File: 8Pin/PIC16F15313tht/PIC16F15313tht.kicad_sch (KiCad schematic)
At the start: 17 parts, among them J1 JACK DC, J2 USB_B, J3 TERMINAL BLOCK, J4 POWER HEADERS, J5 Conn_02x04_Odd_Even, J6 Conn_02x04_Odd_Even, J7 ICSP, SW1 RESET, SW2 CONTROL, U1 PIC16F15313

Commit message: avance de actualización del proyecto
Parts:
- removed J4: POWER HEADERS, Connector_PinSocket_2.54mm:PinSocket_2x02_P2.54mm_Vertical, symbol Connector_Generic:Conn_02x02_Counter_Clockwise
- removed J5: Conn_02x04_Odd_Even, Connector_PinSocket_2.54mm:PinSocket_2x04_P2.54mm_Vertical, symbol Connector_Generic:Conn_02x04_Odd_Even
- removed J7: ICSP, Connector_PinHeader_2.54mm:PinHeader_1x06_P2.54mm_Horizontal, symbol Connector_Generic:Conn_01x06
- removed U1: PIC16F15313, Package_DIP:DIP-8_W7.62mm_Socket_LongPads, symbol MGV:PIC16F15313
- added C1: C, Capacitor_THT:C_Disc_D5.0mm_W2.5mm_P5.00mm, symbol Device:C
- added J4: Conn_02x02_Odd_Even, Connector_PinHeader_2.54mm:PinHeader_2x02_P2.54mm_Vertical, symbol Connector_Generic:Conn_02x02_Odd_Even
- added J5: ICSP, Connector_PinHeader_2.54mm:PinHeader_1x06_P2.54mm_Horizontal, symbol Connector_Generic:Conn_01x06
- added J7: terminales, Connector_PinHeader_2.54mm:PinHeader_2x04_P2.54mm_Vertical, symbol Connector_Generic:Conn_02x04_Odd_Even
- added U1: PIC16F15313, Package_DIP:DIP-8_W7.62mm, symbol CreatedSimbols:PIC16F15313
- D2: value LED_ON -> LED
- D3: value LED_OP -> LED OP
- J1: footprint Connector_BarrelJack:BarrelJack_Kycon_KLDX-0202-xC_Horizontal -> Connector_BarrelJack:BarrelJack_Horizontal
- J2: footprint Connector_USB:USB_B_OST_USB-B1HSxx_Horizontal -> Connector_USB:USB_B_Lumberg_2411_02_Horizontal
- J6: value Conn_02x04_Odd_Even -> terminales; footprint Connector_PinSocket_2.54mm:PinSocket_2x04_P2.54mm_Vertical -> Connector_PinHeader_2.54mm:PinHeader_2x04_P2.54mm_Vertical
- R1: value 10k -> 330
- R2: value 330 -> 10k
- SW1: footprint Button_Switch_THT:SW_PUSH_6mm_H4.3mm -> Button_Switch_THT:SW_PUSH_6mm
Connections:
- net GND: now also C1.2, J5.4 (Pin_4), U1.8 (VSS)
- net VCC: now also C1.1, J5.5 (Pin_5), J7.1 (Pin_1), J7.2 (Pin_2), U1.1 (VDD)
- net on/off: now also J3.1 (Pin_1), J4.2 (Pin_2), J4.4 (Pin_4); no longer J3.2 (Pin_2)
- net pgc: now also J5.2 (Pin_2), U1.6 (RA1/ICSPCLK)
- net pgd: now also J5.3 (Pin_3), U1.7 (RA0/ICSPDAT)
- net ra2: now also U1.5 (RA2)
- net ra3: now also J5.6 (Pin_6), J7.7 (Pin_7), J7.8 (Pin_8), U1.4 (VPP/MCLR/RA3)
- net ra4: now also J7.5 (Pin_5), J7.6 (Pin_6), U1.3 (RA4)
- net ra5: now also J7.3 (Pin_3), J7.4 (Pin_4), U1.2 (RA5)
- net reset: now also R2.2; no longer R1.2
- net at D1.2 (A): now also J3.2 (Pin_2), J4.1 (Pin_1), J4.3 (Pin_3); no longer J3.1 (Pin_1)
- net at D2.2 (A): now also R1.2; no longer R2.2
- new net aux: J5.1 (Pin_1)
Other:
- note removed: "Alimentación"
- note removed: "Microcontrolador"
- note removed: "PIC16F15313"
- note removed: "Periféricos"
- note removed: "Puertos"
- company: MGV 3D -> MGV3D
- title: General PIC16f15313 -> Pecten mi 16F15313

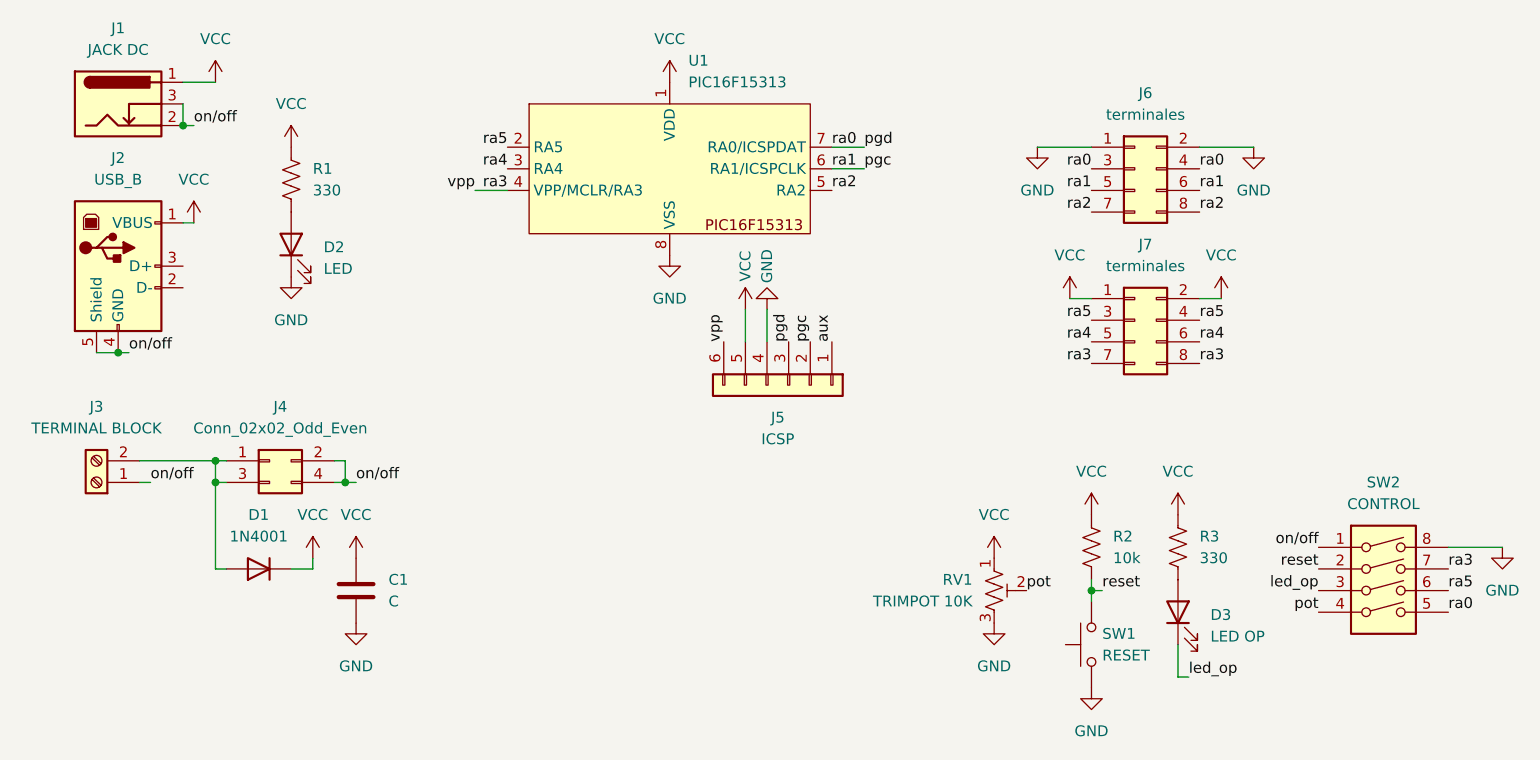
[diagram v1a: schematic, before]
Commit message: Se inicio la creacion de la huella tp4056
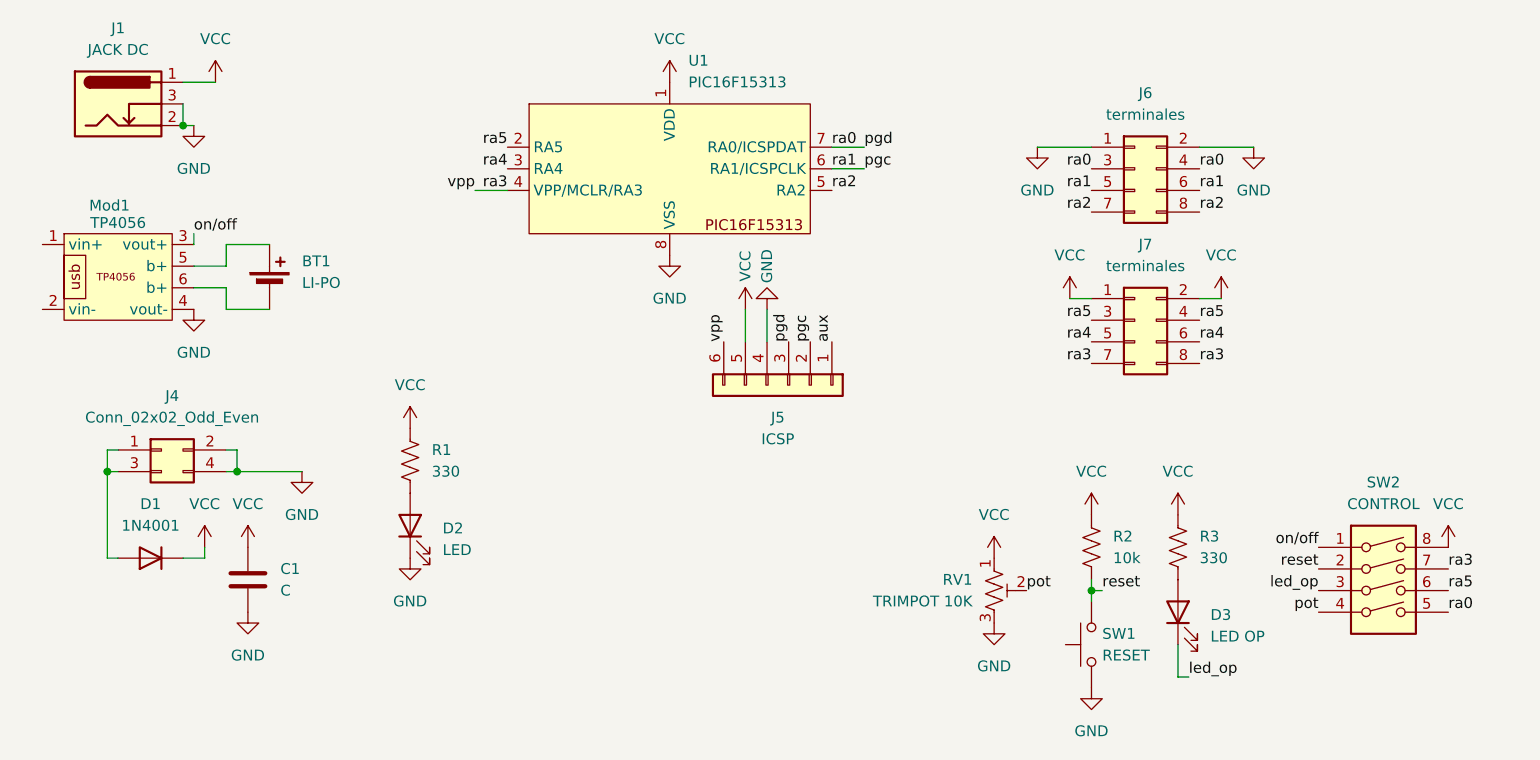
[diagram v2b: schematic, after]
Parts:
- removed J2: USB_B, Connector_USB:USB_B_Lumberg_2411_02_Horizontal, symbol Connector:USB_B
- removed J3: TERMINAL BLOCK, TerminalBlock_Phoenix:TerminalBlock_Phoenix_MKDS-1,5-2-5.08_1x02_P5.08mm_Horizontal, symbol Connector:Screw_Terminal_01x02
- added BT1: LI-PO, symbol Device:Battery_Cell
- added Mod1: TP4056, symbol CreatedSimbols:TP4056
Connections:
- net GND: now also J1.2, J1.3, J4.2 (Pin_2), J4.4 (Pin_4), Mod1.4 (vout-); no longer SW2.8
- net VCC: now also SW2.8
- net on/off: now also Mod1.3 (vout+); no longer J1.2, J1.3, J4.2 (Pin_2), J4.4 (Pin_4)
- new net: BT1.1 (+), Mod1.5 (b+)
- new net: BT1.2 (-), Mod1.6 (b+)
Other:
- moved on the sheet: C1, D1, D2, J4, R1

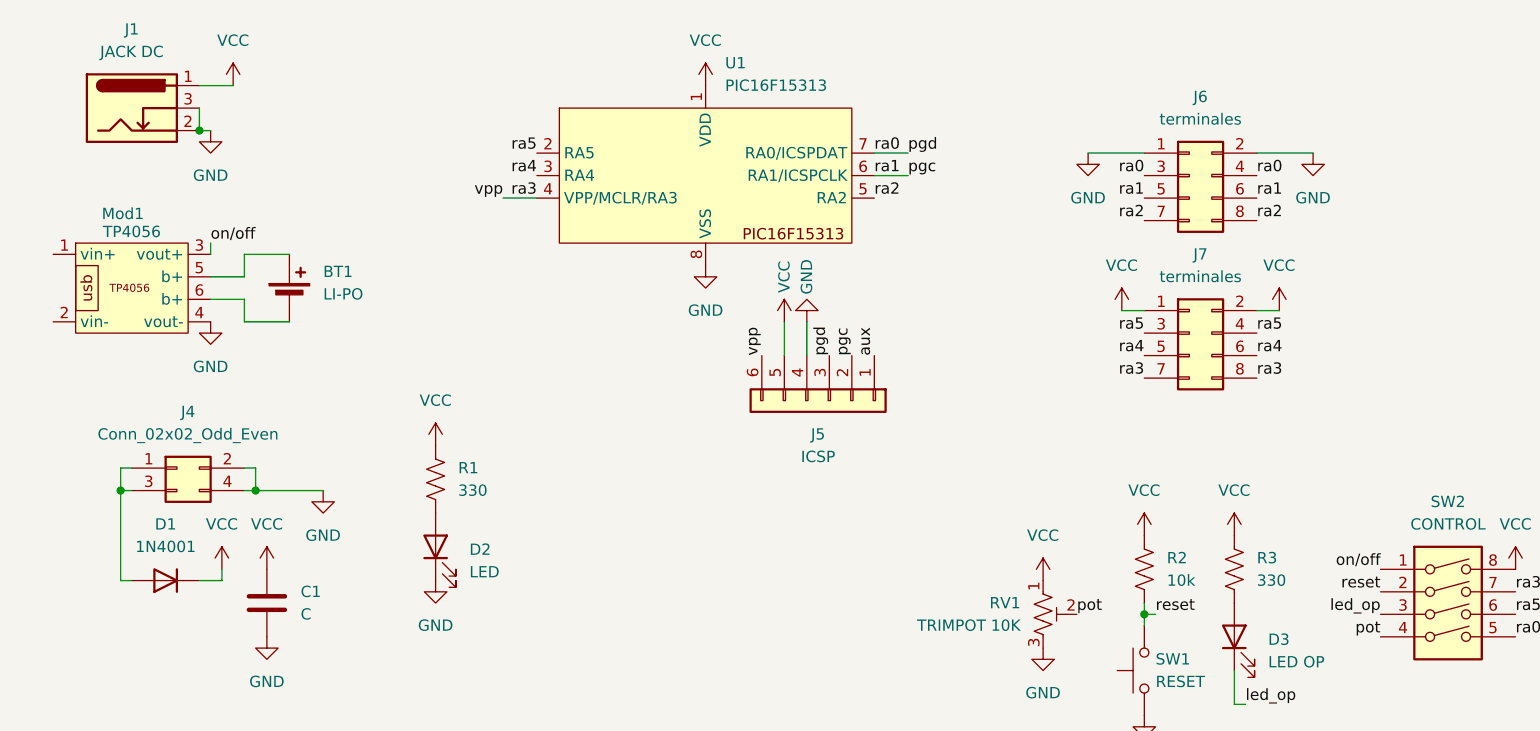
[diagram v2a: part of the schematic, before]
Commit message: Se terminó la huella del tp4056
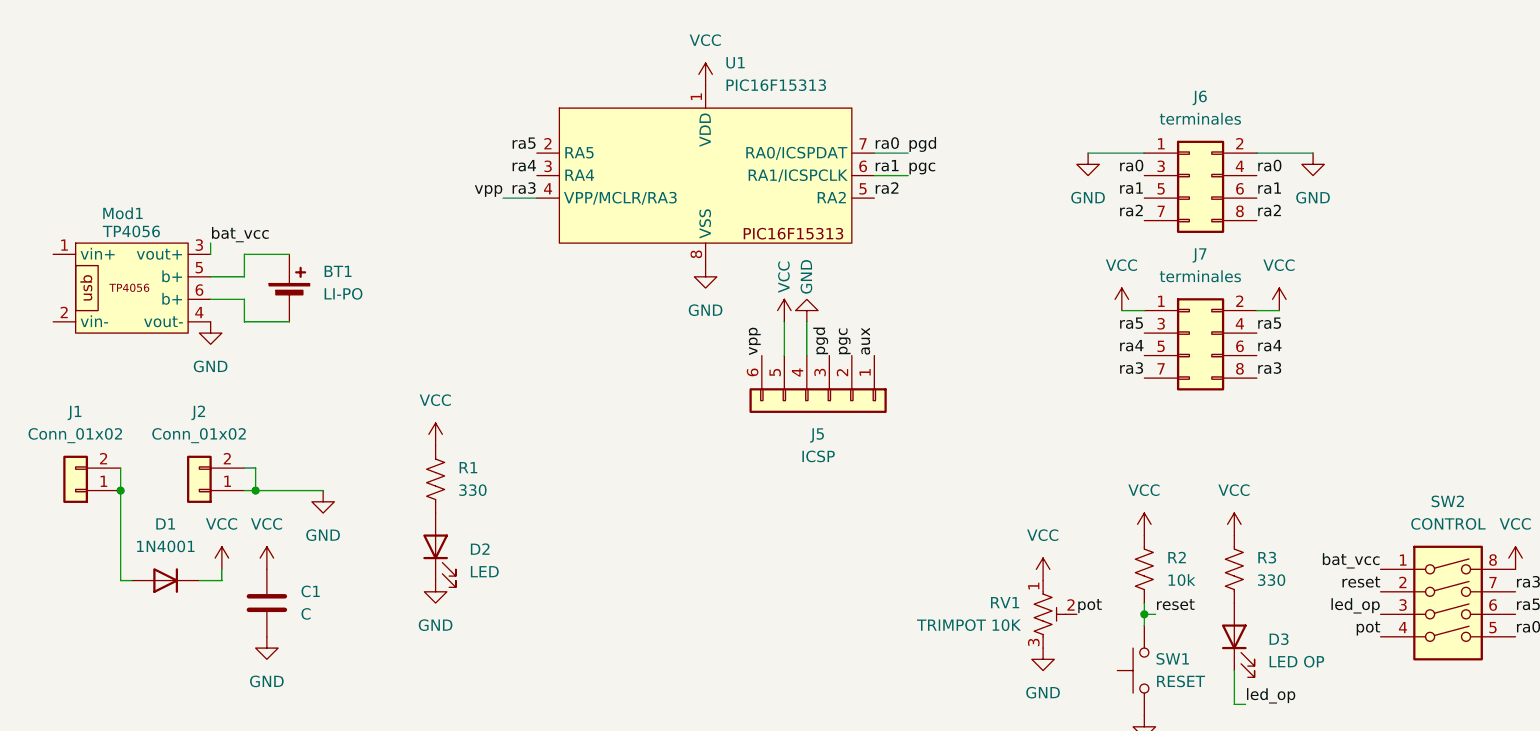
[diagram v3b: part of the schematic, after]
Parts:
- removed J1: JACK DC, Connector_BarrelJack:BarrelJack_Horizontal, symbol Connector:Barrel_Jack_Switch
- removed J4: Conn_02x02_Odd_Even, Connector_PinHeader_2.54mm:PinHeader_2x02_P2.54mm_Vertical, symbol Connector_Generic:Conn_02x02_Odd_Even
- added J1, J2: Conn_01x02, Connector_PinHeader_2.54mm:PinHeader_1x02_P2.54mm_Vertical, symbol Connector_Generic:Conn_01x02
- BT1: footprint (none) -> Connector_PinHeader_2.54mm:PinHeader_1x02_P2.54mm_Vertical_SMD_Pin1Right
- Mod1: footprint (none) -> CreatedFootprints:TP4056
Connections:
- net GND: now also J2.1 (Pin_1), J2.2 (Pin_2)
- net at D1.2 (A): now also J1.1 (Pin_1), J1.2 (Pin_2)
- net on/off renamed bat_vcc

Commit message: finalizacion de la tarjeta
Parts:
- removed BT1: LI-PO, Connector_PinHeader_2.54mm:PinHeader_1x02_P2.54mm_Vertical_SMD_Pin1Right, symbol Device:Battery_Cell
- added J3, J4: Conn_01x01, TestPoint:TestPoint_Pad_D2.5mm, symbol Connector_Generic:Conn_01x01
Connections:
- net GND: now also J1.2 (Pin_2); no longer J2.1 (Pin_1)
- net at Mod1.5 (b+): now also J3.1 (Pin_1)
- net at Mod1.6 (b+): now also J4.1 (Pin_1)
- net at D1.2 (A), J1.1 (Pin_1): now also J2.1 (Pin_1); no longer J1.2 (Pin_2)
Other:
- moved on the sheet: J1, J2
